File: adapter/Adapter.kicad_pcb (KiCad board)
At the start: 4 copper layers, 52 parts, among them J1 USB_B_Micro, J2 2040210-1, J3 USB_C_Receptacle, J4 Conn_01x05_Male, J5 Conn_01x03_Male, Q1 IRLML2244TRPBF, SW1 SW_Push, SW2 SW_Push, U1 SN75DP119, U2 AZ1117-3.3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

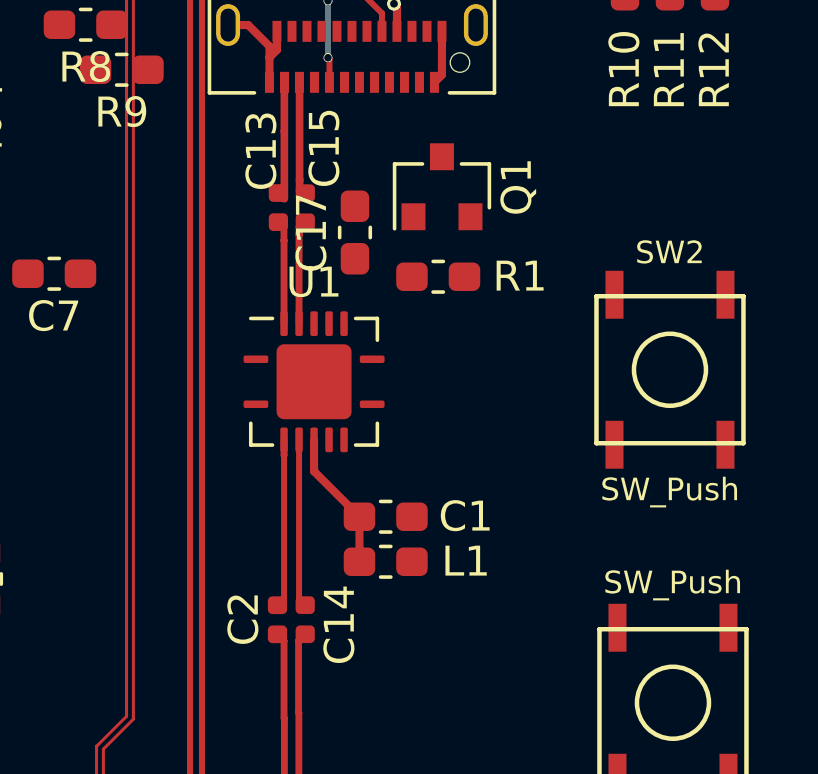
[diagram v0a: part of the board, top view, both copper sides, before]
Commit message: remove the bead for the DP119
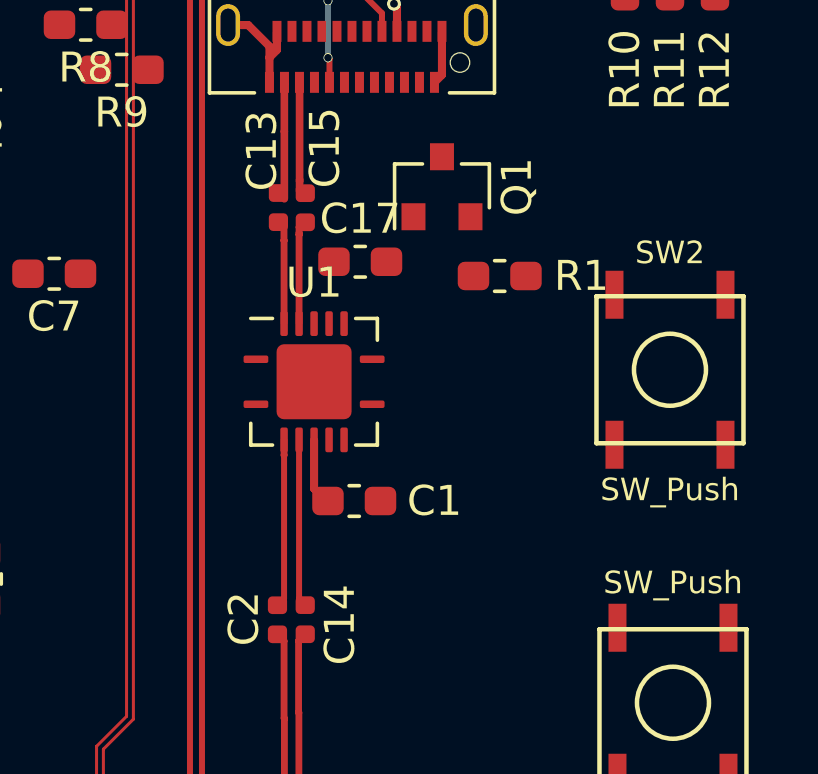
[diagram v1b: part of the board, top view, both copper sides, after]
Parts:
- removed L1: CIM05U601NC, Inductor_SMD:L_0603_1608Metric_Pad1.05x0.95mm_HandSolder
- moved R1 2.05 mm to (61.1, 50.3)
- moved C1 1.17 mm to (56.3, 57.8)
- moved C17 0.99 mm to (56.5, 49.8), turned to 0 degrees
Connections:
- C1 pad 1: Net-(C1-Pad1) -> +3V3
- C17 pad 1: Net-(C1-Pad1) -> +3V3
- U1 pad 11: Net-(C1-Pad1) -> +3V3
- U1 pad 4: Net-(C1-Pad1) -> +3V3
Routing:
- net Net-(C1-Pad1): track 4.69 -> 0.00 mm
- net +3V3: track 0.00 -> 2.21 mm

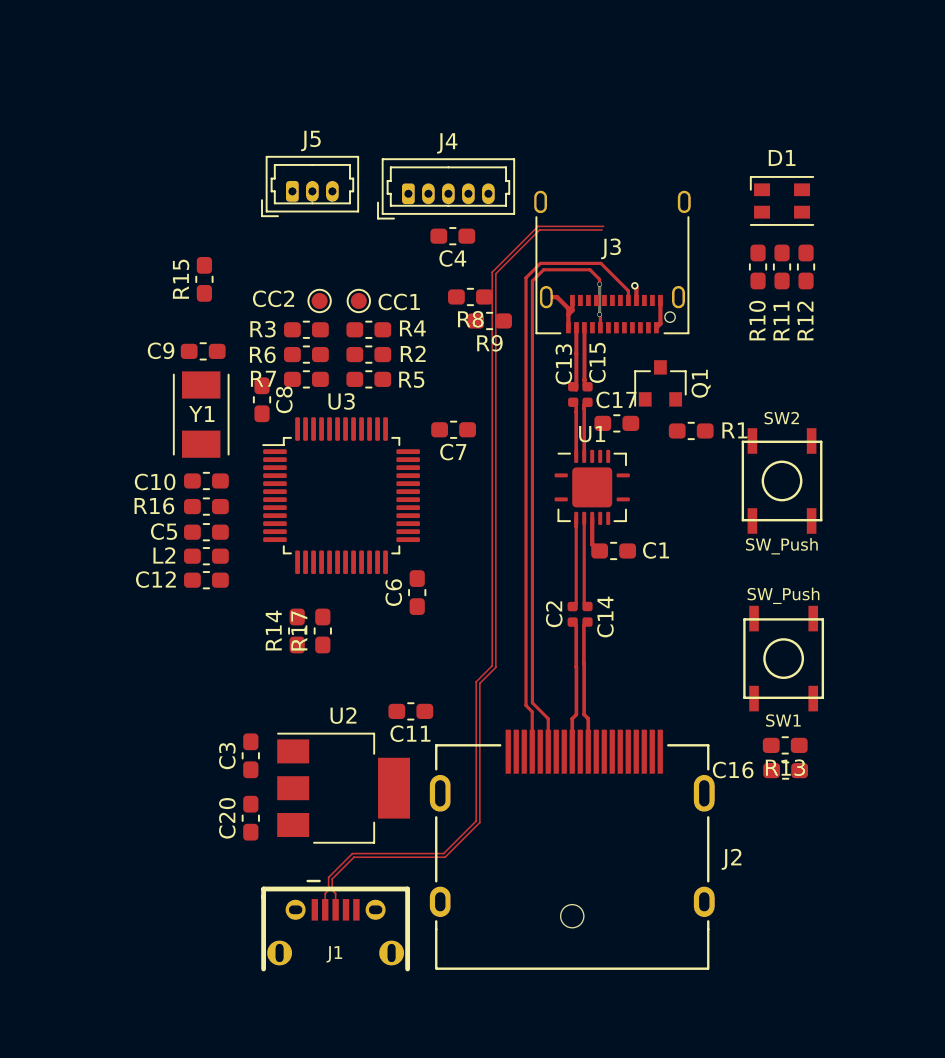
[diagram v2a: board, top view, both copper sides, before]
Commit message: Replaced SN75DP119 symbol/footprint with premade one from Arrow librarian
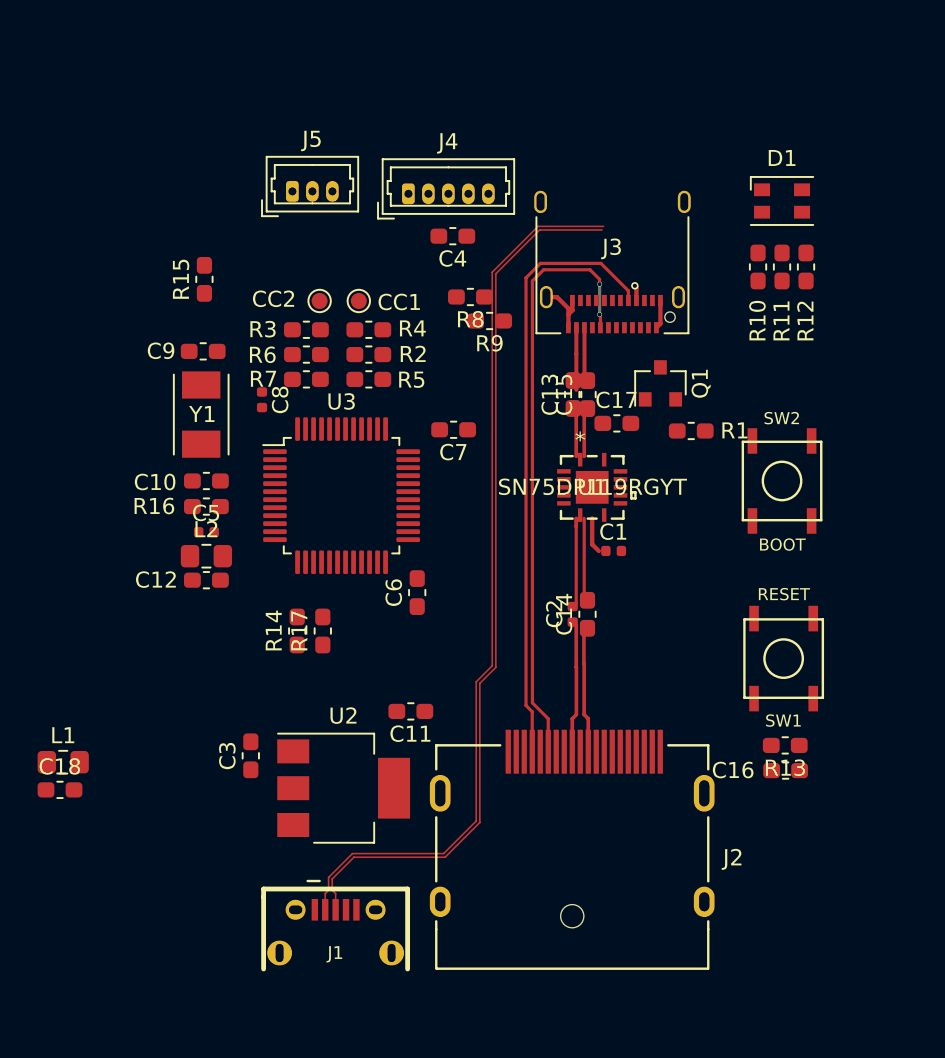
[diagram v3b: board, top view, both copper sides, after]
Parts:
- removed C20: 4u7, Capacitor_SMD:C_0603_1608Metric_Pad1.05x0.95mm_HandSolder
- added C18: 100n, Capacitor_SMD:C_0603_1608Metric_Pad1.05x0.95mm_HandSolder, F.Cu at (21.7, 72.7)
- added L1: MH2029-300Y, Inductor_SMD:L_0805_2012Metric_Pad1.15x1.40mm_HandSolder, F.Cu at (21.9, 71.0)
- C1, C5, C8: footprint Capacitor_SMD:C_0603_1608Metric_Pad1.05x0.95mm_HandSolder -> Capacitor_SMD:C_0402_1005Metric
- C12: value 1u -> 4u7
- C13, C14, C15: footprint Capacitor_SMD:C_0402_1005Metric -> Capacitor_SMD:C_0603_1608Metric_Pad1.05x0.95mm_HandSolder
- L2: value CIM05U601NC -> MH2029-300Y; footprint Inductor_SMD:L_0603_1608Metric_Pad1.05x0.95mm_HandSolder -> Inductor_SMD:L_0805_2012Metric_Pad1.15x1.40mm_HandSolder
- SW1: value SW_Push -> RESET
- SW2: value SW_Push -> BOOT
- U1: value SN75DP119 -> SN75DP119RGYT; footprint SN75DP119:QFN-20-1EP_4x4mm_P0.5mm_EP2.5x2.5mm -> SN75DP119:SN75DP119RGYT
- U2: value AZ1117-3.3 -> LD1117S33TR
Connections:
- C1 pad 1: +3V3 -> Net-(C1-Pad1)
- C1 pad 2: GND -> /DP_OUT_0+
- C11 pad 2: +3V3 -> VDD
- C13 pad 1: Net-(C13-Pad1) -> GND
- C13 pad 2: /DP_OUT_0+ -> +3V3
- C14 pad 1: /DP_IN_0- -> GND
- C14 pad 2: Net-(C14-Pad2) -> +3V3
- C15 pad 1: Net-(C15-Pad1) -> GND
- C15 pad 2: /DP_OUT_0- -> VDD
- C17 pad 1: +3V3 -> GND
- C17 pad 2: GND -> VDD
- C5 pad 1: GND -> Net-(C5-Pad1)
- C5 pad 2: VDDA -> /DP_OUT_0-
- C6 pad 2: +3V3 -> VDD
- C7 pad 1: GND -> VBUS
- C7 pad 2: +3V3 -> GND
- C8 pad 1: GND -> /DP_IN_0-
- C8 pad 2: +3V3 -> Net-(C8-Pad2)
- U1 pad 12: Net-(C15-Pad1) -> Net-(C1-Pad1)
- U1 pad 13: Net-(C13-Pad1) -> Net-(C5-Pad1)
- U1 pad 2: Net-(C2-Pad2) -> Net-(C8-Pad2)
- U1 pad 3: Net-(C14-Pad2) -> Net-(C2-Pad2)
- U3 pad 1: +3V3 -> VDD
- U3 pad 24: +3V3 -> VDD
- U3 pad 36: +3V3 -> VDD
- U3 pad 48: +3V3 -> VDD
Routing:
- net GND: track 5.65 -> 12.8 mm
- net Net-(C14-Pad2): track 5.59 -> 0.00 mm
- net +3V3: track 2.21 -> 7.80 mm
- net Net-(C15-Pad1): track 3.61 -> 0.00 mm
- net Net-(C13-Pad1): track 3.58 -> 0.00 mm

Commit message: cleared all order number for Arrow
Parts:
- added R18: 1M, Resistor_SMD:R_0603_1608Metric_Pad1.05x0.95mm_HandSolder, F.Cu at (32.2, 67.4)
- added R19: 1M, Resistor_SMD:R_0603_1608Metric_Pad1.05x0.95mm_HandSolder, F.Cu at (32.2, 65.9)
- C10, C9: value 20p -> 12p
- R10: value R -> 806
- R11: value R -> 576
- R12: value R -> 604
- R15: value 100k -> 0
- R2, R3: value <5k? -> 1k7
- R8: value 0 -> 100k
- SW1: value RESET -> BOOT
- moved C18 2.50 mm to (24.1, 72.0)
- moved L1 2.50 mm to (24.3, 70.3)
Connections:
- C4 pad 1: /nRESET -> GND
- C4 pad 2: GND -> /nRESET
- R13 pad 1: +3V3 -> /BOOT
- R13 pad 2: /nRESET -> GND
- R15 pad 1: /BOOT -> /D-
- R15 pad 2: GND -> Net-(R15-Pad2)
- R17 pad 1: /AUX+ -> /D+
- R8 pad 1: /D- -> +3V3
- R8 pad 2: Net-(R8-Pad2) -> /nRESET
- R9 pad 1: /D+ -> /AUX+
- U3 pad 15: Net-(R17-Pad2) -> Net-(R9-Pad2)
- U3 pad 32: Net-(R8-Pad2) -> Net-(R15-Pad2)
- U3 pad 33: Net-(R9-Pad2) -> Net-(R17-Pad2)

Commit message: placement mostly done
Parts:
- added MH1: MountingHole, MountingHole:MountingHole_2.5mm, F.Cu at (29.5, 80.0)
- added MH2: MountingHole, MountingHole:MountingHole_2.5mm, F.Cu at (29.5, 37.0)
- added MH3: MountingHole, MountingHole:MountingHole_2.5mm, F.Cu at (67.5, 80.0)
- added MH4: MountingHole, MountingHole:MountingHole_2.5mm, F.Cu at (67.5, 36.5)
- J4: footprint Connector_Molex:Molex_PicoBlade_53047-0510_1x05_P1.25mm_Vertical -> Connector_PinHeader_2.54mm:PinHeader_1x05_P2.54mm_Horizontal
- J5: footprint Connector_Molex:Molex_PicoBlade_53047-0310_1x03_P1.25mm_Vertical -> Connector_PinHeader_2.54mm:PinHeader_1x03_P2.54mm_Horizontal; moved to B.Cu
- R18: value 1M -> 97.6
- R5: value 100 -> 97.6
- R7: value 100 -> 1M
- SW1: value BOOT -> RESET
- U2: footprint Package_TO_SOT_SMD:SOT-223 -> Package_TO_SOT_SMD:SOT-223-3_TabPin2
- moved C7 27.1 mm to (33.6, 74.1), turned to 90 degrees
- moved C15 26.8 mm to (31.1, 60.9), turned to 0 degrees
- moved R15 26.6 mm to (40.2, 65.6)
- moved C18 25.6 mm to (34.5, 48.6), turned to 270 degrees
- moved C5 25.0 mm to (53.8, 46.7), turned to 90 degrees
- moved R7 24.5 mm to (53.0, 65.6), turned to 90 degrees
- moved CC2 24.3 mm to (62.1, 39.6), turned to 0 degrees
- moved C8 23.6 mm to (53.7, 61.7), turned to 90 degrees
- moved R14 22.2 mm to (50.3, 45.4), turned to 180 degrees
- moved R19 19.3 mm to (51.5, 65.6), turned to 90 degrees
- moved C17 16.9 mm to (45.3, 62.5), turned to 90 degrees
- moved CC1 16.8 mm to (56.6, 46.2), turned to 90 degrees
- moved C9 16.2 mm to (46.5, 48.6), turned to 270 degrees
- moved C11 15.1 mm to (31.1, 59.3), turned to 0 degrees
- moved R3 15.1 mm to (31.1, 57.8), turned to 180 degrees
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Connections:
- C1 pad 2: /DP_OUT_0+ -> /DP_OUT_0-
- C2 pad 1: /DP_IN_0+ -> /DP_IN_0-
- C5 pad 2: /DP_OUT_0- -> /DP_OUT_0+
- C8 pad 1: /DP_IN_0- -> /DP_IN_0+
- R18 pad 1: /CONFIG1 -> /CC2_TX
- R18 pad 2: GND -> /CC2
- R7 pad 1: /CC2_TX -> /CONFIG1
- R7 pad 2: /CC2 -> GND
- U3 pad 11: /CC1_RX -> EQ_CTL
- U3 pad 13: /CC2_RX -> VOD_CTL
- U3 pad 17: VOD_CTL -> /TX_CLK
- U3 pad 18: EQ_CTL -> /CC1_RX
- U3 pad 19: /TX_CLK -> /CC2_RX
- U3 pad 20: Net-(U3-Pad20) -> /CC2_EN
- U3 pad 42: /CC2_EN -> Net-(U3-Pad42)
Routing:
- net /nRESET: track 0.00 -> 41.6 mm, vias 0 -> 1
- net GND: track 12.8 -> 42.5 mm, vias 0 -> 18
- net /BOOT: track 0.00 -> 25.7 mm, vias 0 -> 2
- net +3V3: track 7.80 -> 32.4 mm, vias 0 -> 6
- net /HPD: track 0.00 -> 18.0 mm, vias 0 -> 2
- net /TX_CLK: track 0.00 -> 17.3 mm, vias 0 -> 2
- net VBUS: track 0.00 -> 11.1 mm, vias 0 -> 3
- net Net-(C9-Pad1): track 0.00 -> 10.9 mm
- net /CC2: track 0.00 -> 9.12 mm, vias 0 -> 2
- net Net-(J3-PadA4): track 0.96 -> 7.63 mm, vias 1 -> 5
- net VDDA: track 0.00 -> 5.94 mm
- net Net-(C8-Pad2): track 0.00 -> 5.48 mm
- net Net-(R17-Pad2): track 0.00 -> 5.42 mm
- net Net-(C5-Pad1): track 0.00 -> 5.15 mm
- net Net-(C1-Pad1): track 0.00 -> 5.14 mm
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- added copper zone on In2.Cu, net +3V3
- added copper zone on In1.Cu, net GND
- added copper zone on In2.Cu, net GND
- added copper zone on In2.Cu, net Net-(J3-PadA4)
- added copper zone on In2.Cu, net VBUS
- added copper zone on In2.Cu, net VDD
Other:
- board outline added: 45.5 x 51 mm
- board text added: "3.3V"
- board text added: "GND"
- board text added: "RESET"
- board text added: "SWCLK"
- board text added: "SWDIO"

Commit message: first fully routed
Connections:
- U3 pad 17: /TX_CLK -> Net-(U3-Pad17)
- U3 pad 21: VBUS_EN -> Net-(U3-Pad21)
- U3 pad 45: Net-(U3-Pad45) -> /TX_CLK
- U3 pad 46: Net-(U3-Pad46) -> VBUS_EN
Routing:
- net /LED_G_L: track 0.00 -> 43.6 mm, vias 0 -> 2
- net /CC1: track 0.00 -> 42.5 mm, vias 0 -> 3
- net /CC2: track 9.12 -> 51.4 mm
- net /nRESET: track 41.6 -> 81.8 mm, vias 1 -> 3
- net /SWDIO: track 0.00 -> 40.0 mm, vias 0 -> 1
- net /LED_R_L: track 0.00 -> 39.9 mm, vias 0 -> 2
- net /LED_B_L: track 0.00 -> 39.5 mm, vias 0 -> 2
- net /UART_RX: track 0.00 -> 38.1 mm, vias 0 -> 1
- net /SWCLK: track 0.00 -> 33.0 mm, vias 0 -> 1
- net EQ_CTL: track 0.00 -> 32.1 mm, vias 0 -> 2
- net EN_CTL: track 0.00 -> 31.3 mm, vias 0 -> 2
- net /UART_TX: track 0.00 -> 29.2 mm, vias 0 -> 2
- net PRE_CTL: track 0.00 -> 24.5 mm, vias 0 -> 2
- net GND: track 42.5 -> 67.1 mm, vias 18 -> 33
- net VOD_CTL: track 0.00 -> 22.2 mm, vias 0 -> 2
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
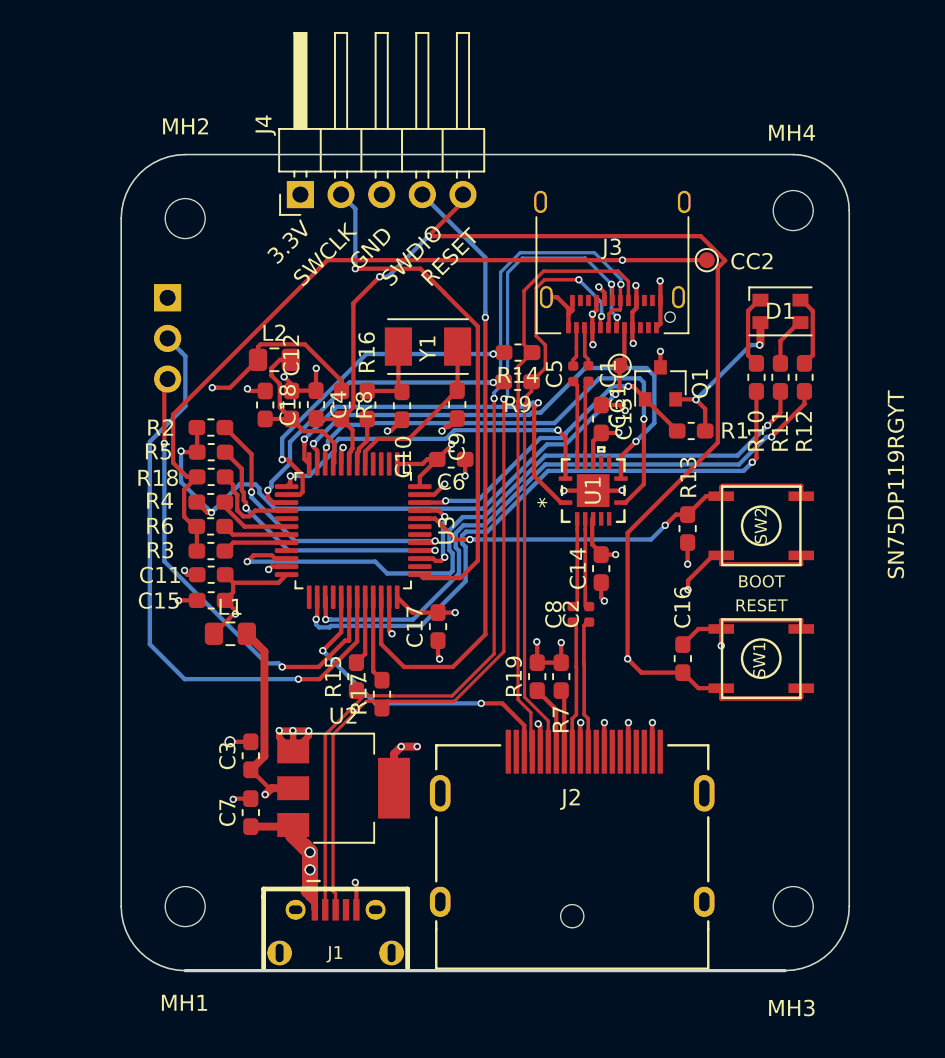
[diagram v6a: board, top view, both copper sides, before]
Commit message: shifting back some components from the USB-C jack
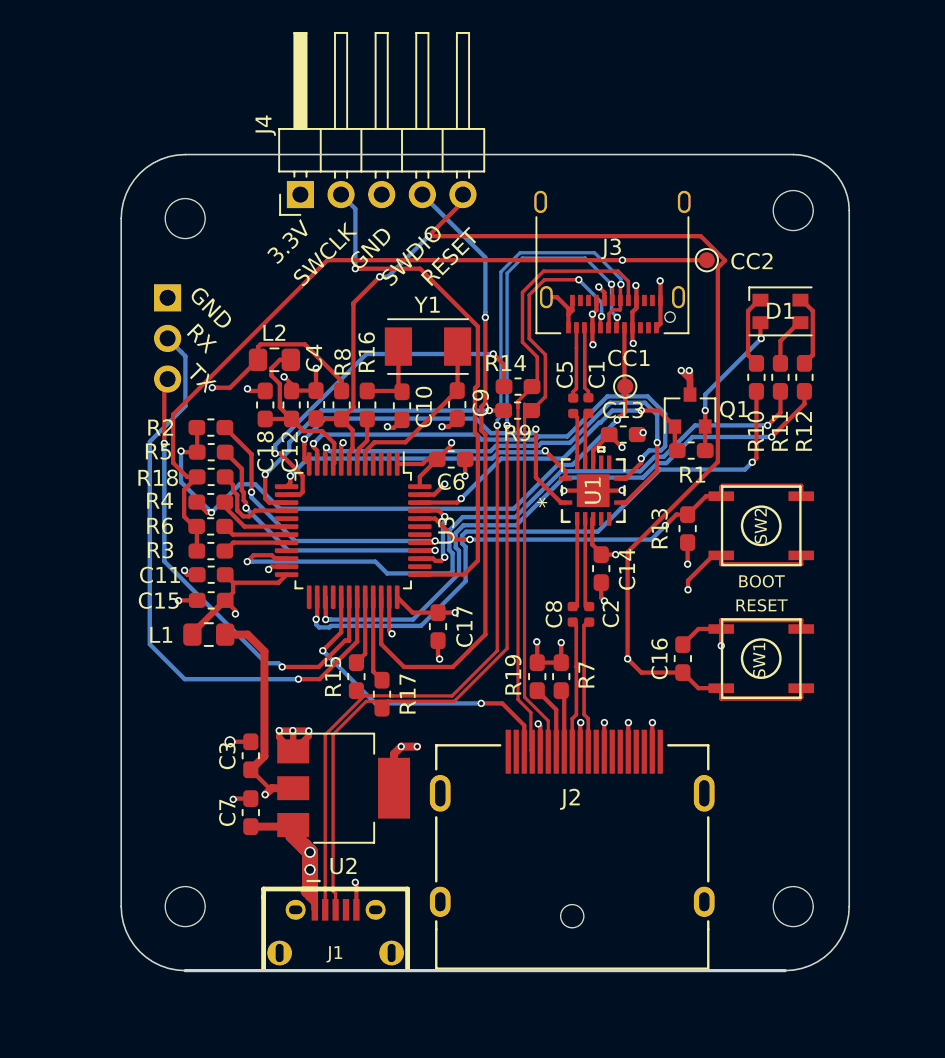
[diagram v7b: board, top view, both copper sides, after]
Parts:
- moved Q1 2.51 mm to (61.0, 49.0)
- moved R14 2.12 mm to (50.3, 47.5)
- moved C1 2.00 mm to (54.7, 48.7)
- moved C5 2.00 mm to (53.8, 48.7)
- moved R9 1.80 mm to (50.3, 49.0)
- moved C13 1.69 mm to (56.9, 50.5), turned to 180 degrees
- moved L1 1.35 mm to (31.0, 63.0)
- moved CC1 1.35 mm to (57.0, 47.5)
- moved R1 1.23 mm to (61.1, 51.5)
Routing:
- net VOD_CTL: track 22.2 -> 19.6 mm
- net Net-(J3-PadA4): track 7.63 -> 9.88 mm, vias 5 -> 6
- net Net-(R14-Pad2): track 21.3 -> 23.3 mm
- net Net-(C5-Pad1): track 5.15 -> 3.15 mm
- net /DP_OUT_0-: track 2.53 -> 4.53 mm
- net /DP_OUT_0+: track 2.54 -> 4.54 mm
- net Net-(C1-Pad1): track 5.14 -> 3.14 mm
- net PRE_CTL: track 24.5 -> 22.7 mm
- net +3V3: track 43.7 -> 45.2 mm
- net VDD: track 18.6 -> 20.0 mm
- net EN_CTL: track 31.3 -> 30.0 mm
- net /CC1: track 42.5 -> 43.7 mm
- net EQ_CTL: track 32.1 -> 31.1 mm
- net GND: track 67.1 -> 66.0 mm
- net VBUS: track 20.0 -> 19.2 mm
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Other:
- board text added: "RX"
- board text added: "TX"

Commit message: Connect EXT3.3V to 3.3V
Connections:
- J4 pad 1: /EXT_3.3V -> +3V3
